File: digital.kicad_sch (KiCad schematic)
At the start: 0 parts

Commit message: new OpAmp, new RC calc, G431 added
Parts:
- added C21: 10u, symbol Device:C
- added C22, C23, C24, C25, C26, C27, C29, C31: 100n, symbol Device:C
- added C28, C30: 1u, symbol Device:C
- added C32, C33: 20p, symbol Device:C
- added J8: Conn_01x05, Connector_PinHeader_2.54mm:PinHeader_1x05_P2.54mm_Vertical, symbol Connector_Generic:Conn_01x05
- added R19: 390R, symbol Device:R
- added R20, R21, R22: 10R, symbol Device:R
- added SW1: RST, Button_Switch_SMD:SW_MEC_5GSH9, symbol Switch:SW_MEC_5E
- added U8: STM32G431RBT6, Package_QFP:LQFP-64_10x10mm_P0.5mm, symbol MCU_ST_STM32G4:STM32G431RBTx
- added Y1: Crystal, symbol Device:Crystal
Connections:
- new net: C33.1, R19.2, Y1.2
- new net: J8.1 (Pin_1), R20.2
- new net: J8.2 (Pin_2), R21.2
- new net: J8.3 (Pin_3), R22.2
- new net +3.3V: C21.1, C22.1, C23.1, C24.1, C25.1, C26.1, U8.1 (VBAT), U8.16 (VDD), U8.32 (VDD), U8.48 (VDD), U8.64 (VDD)
- new net +3.3VA: C27.1, C28.1, U8.29 (VDDA)
- new net GND: C21.2, C22.2, C23.2, C24.2, C25.2, C26.2, C27.2, C28.2, C29.2, C30.2, C31.2, C32.2, C33.2, J8.5 (Pin_5), SW1.1, SW1.2, U8.15 (VSS), U8.27 (VSSA), U8.31 (VSS), U8.47 (VSS), U8.63 (VSS)
- new net MCU_OSC_IN: C32.1, U8.5 (PF0), Y1.1
- new net MCU_OSC_OUT: R19.1, U8.6 (PF1)
- new net MCU_RST: C31.1, J8.4 (Pin_4), SW1.3 (K), SW1.4 (A), U8.7 (PG10)
- new net MCU_SWCLK: R21.1, U8.50 (PA14)
- new net MCU_SWDIO: R20.1, U8.49 (PA13)
- new net MCU_SWO: R22.1, U8.56 (PB3)
- new net mcu_vref: C29.1, C30.1, U8.28 (VREF+)

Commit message: MCU analog perephery, TL494 FB wiring
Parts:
- added FB2: FB, Inductor_SMD:L_1206_3216Metric, symbol Device:FerriteBead_Small
- added R23: 10K, symbol Device:R
- Y1: value Crystal -> 8MHz
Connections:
- net +3.3V: now also FB2.2
- net GND: now also R23.2
- net MCU_ADC_U: now reaches U8.12 (PA0)
- net MCU_ADC_I: now reaches U8.13 (PA1)
- net MCU_DAC_U: now reaches U8.18 (PA4)
- net MCU_DAC_I: now reaches U8.19 (PA5)
- net MCU_DCH: now reaches U8.24 (PB0)
- net mcu_boot0: now reaches U8.61 (PB8)
- net mcu_boot0: now also R23.1
- net +3.3VA: no longer names the net of C27.1, C28.1, U8.29 (VDDA)
- net +3.3VA: now also FB2.1

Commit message: assign footprints
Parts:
- removed R20, R21, R22: 10R, symbol Device:R
- C21, C28, C30, C32, C33: footprint (none) -> Capacitor_SMD:C_1206_3216Metric_Pad1.33x1.80mm_HandSolder
- C22, C23, C24, C25, C26, C27, C29, C31: footprint (none) -> Capacitor_SMD:C_0805_2012Metric_Pad1.18x1.45mm_HandSolder
- FB2: footprint Inductor_SMD:L_1206_3216Metric -> Inductor_SMD:L_1206_3216Metric_Pad1.22x1.90mm_HandSolder
- R19: value 390R -> 0R; footprint (none) -> Resistor_SMD:R_1206_3216Metric_Pad1.30x1.75mm_HandSolder
- R23: footprint (none) -> Resistor_SMD:R_1206_3216Metric_Pad1.30x1.75mm_HandSolder
- SW1: footprint Button_Switch_SMD:SW_MEC_5GSH9 -> Button_Switch_SMD:SW_Push_1P1T_NO_E-Switch_TL3301NxxxxxG
- Y1: footprint (none) -> Crystal:Crystal_SMD_MicroCrystal_CC1V-T1A-2Pin_8.0x3.7mm_HandSoldering
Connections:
- net MCU_SWCLK: now also J8.2 (Pin_2)
- net MCU_SWDIO: now also J8.1 (Pin_1)
- net MCU_SWO: now also J8.3 (Pin_3)
- net MCU_494_ON: now reaches U8.45 (PA11)
- no-connect marks 0 -> 39

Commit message: approximate location of the components at the PCB
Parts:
- removed SW1: RST, Button_Switch_SMD:SW_Push_1P1T_NO_E-Switch_TL3301NxxxxxG, symbol Switch:SW_MEC_5E
- added SW2: RST, Button_Switch_SMD:SW_Push_1P1T_NO_E-Switch_TL3301NxxxxxG, symbol Switch:SW_Push
- J8: value Conn_01x05 -> SWD
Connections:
- net GND: now also SW2.1
- net MCU_RST: now also J8.1 (Pin_1), SW2.2; no longer J8.4 (Pin_4)
- net MCU_SWCLK: now also J8.3 (Pin_3); no longer J8.2 (Pin_2)
- net MCU_SWDIO: now also J8.2 (Pin_2); no longer J8.1 (Pin_1)
- net MCU_SWO: now also J8.4 (Pin_4); no longer J8.3 (Pin_3)
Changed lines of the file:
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@@
 	)
 	(junction
-		(at 30.48 67.31)
-		(diameter 0)
-		(color 0 0 0 0)
-	)
-	(junction
 		(at 156.21 25.4)
 		(diameter 0)
@@
 	)
 	(junction
-		(at 43.18 67.31)
-		(diameter 0)
-		(color 0 0 0 0)
-	)
-	(junction
 		(at 95.25 25.4)
 		(diameter 0)
@@
 	(wire
 		(pts
-			(xy 30.48 67.31) (xy 30.48 69.85)
+			(xy 30.48 60.96) (xy 30.48 69.85)
 		)
 		(stroke
@@
 	(wire
 		(pts
-			(xy 31.75 67.31) (xy 30.48 67.31)
-		)
-		(stroke
-			(width 0)
-			(type default)
-		)
-	)
-	(wire
-		(pts
 			(xy 46.99 86.36) (xy 72.39 86.36)
 		)
@@
 	(wire
 		(pts
-			(xy 43.18 69.85) (xy 43.18 67.31)
+			(xy 43.18 60.96) (xy 43.18 69.85)
 		)
 		(stroke
@@
 	(wire
 		(pts
-			(xy 43.18 67.31) (xy 41.91 67.31)
-		)
-		(stroke
-			(width 0)
-			(type default)
-		)
-	)
-	(wire
-		(pts
 			(xy 46.99 101.6) (xy 41.91 101.6)
 		)
@@
 	(wire
 		(pts
-			(xy 30.48 60.96) (xy 30.48 67.31)
-		)
-		(stroke
-			(width 0)
-			(type default)
-		)
-	)
-	(wire
-		(pts
 			(xy 134.62 25.4) (xy 143.51 25.4)
 		)
@@
 		)
 	)
-	(wire
-		(pts
-			(xy 43.18 67.31) (xy 43.18 60.96)
-		)
-		(stroke
-			(width 0)
-			(type default)
-		)
-	)
 	(label "mcu_boot0"
 		(at 157.48 120.65 0)
@@
 	(global_label "MCU_SWO"
 		(shape input)
-		(at 238.76 31.75 180)
+		(at 238.76 34.29 180)
 		(fields_autoplaced yes)
 		(effects
@@
 		)
 		(property "Intersheetrefs" "${INTERSHEET_REFS}"
-			(at 226.7639 31.75 0)
+			(at 226.7639 34.29 0)
 			(effects
 				(font
@@
 	(global_label "MCU_SWDIO"
 		(shape input)
-		(at 238.76 26.67 180)
+		(at 238.76 29.21 180)
 		(fields_autoplaced yes)
 		(effects
@@
 		)
 		(property "Intersheetrefs" "${INTERSHEET_REFS}"
-			(at 224.8891 26.67 0)
+			(at 224.8891 29.21 0)
 			(effects
 				(font
@@
 	(global_label "MCU_SWCLK"
 		(shape input)
-		(at 238.76 29.21 180)
+		(at 238.76 31.75 180)
 		(fields_autoplaced yes)
 		(effects
@@
 		)
 		(property "Intersheetrefs" "${INTERSHEET_REFS}"
-			(at 224.5263 29.21 0)
+			(at 224.5263 31.75 0)
 			(effects
 				(font
@@
 	(global_label "MCU_RST"
 		(shape input)
-		(at 238.76 34.29 180)
+		(at 238.76 26.67 180)
 		(fields_autoplaced yes)
 		(effects
@@
 		)
 		(property "Intersheetrefs" "${INTERSHEET_REFS}"
-			(at 227.3082 34.29 0)
+			(at 227.3082 26.67 0)
 			(effects
 				(font
@@
 	)
 	(symbol
+		(lib_id "Switch:SW_Push")
+		(at 36.83 69.85 0)
+		(unit 1)
+		(exclude_from_sim no)
+		(in_bom yes)
+		(on_board yes)
+		(dnp no)
+		(fields_autoplaced yes)
+		(property "Reference" "SW2"
+			(at 36.83 62.23 0)
+			(effects
+				(font
+					(size 1.27 1.27)
+				)
+			)
+		)
+		(property "Value" "RST"
+			(at 36.83 64.77 0)
+			(effects
+				(font
+					(size 1.27 1.27)
+				)
+			)
+		)
+		(property "Footprint" "Button_Switch_SMD:SW_Push_1P1T_NO_E-Switch_TL3301NxxxxxG"
+			(at 36.83 64.77 0)
+			(effects
+				(font
+					(size 1.27 1.27)
+				)
+				(hide yes)
+			)
+		)
+		(property "Datasheet" "~"
+			(at 36.83 64.77 0)
+			(effects
+				(font
+					(size 1.27 1.27)
+				)
+				(hide yes)
+			)
+		)
+		(property "Description" "Push button switch, generic, two pins"
+			(at 36.83 69.85 0)
+			(effects
+				(font
+					(size 1.27 1.27)
+				)
+				(hide yes)
+			)
+		)
+		(pin "1"
+		)
+		(pin "2"
+		)
+		(instances
+			(project ""
+				(path "/485c2fed-5176-4ba8-b79d-ac7eddb44491/422ff71a-ee59-41d3-a8e4-e6d2465802f7"
+					(reference "SW2")
+					(unit 1)
+				)
+			)
+		)
+	)
+	(symbol
 		(lib_id "Device:C")
 		(at 68.58 62.23 0)
@@
 			)
 		)
-		(property "Value" "Conn_01x05"
+		(property "Value" "SWD"
 			(at 252.73 33.0199 0)
 			(effects
@@
 					(unit 1)
 				)
-			)
-		)
-	)
-	(symbol
-		(lib_id "Switch:SW_MEC_5E")
-		(at 36.83 69.85 0)
-		(unit 1)
-		(exclude_from_sim no)
-		(in_bom yes)
-		(on_board yes)
-		(dnp no)
-		(property "Reference" "SW1"
-			(at 34.798 71.628 0)
-			(effects
-				(font
-					(size 1.27 1.27)
-				)
-				(justify left)
-			)
-		)
-		(property "Value" "RST"
-			(at 34.798 74.168 0)
-			(effects
-				(font
-					(size 1.27 1.27)
-				)
-				(justify left)
-			)
-		)
-		(property "Footprint" "Button_Switch_SMD:SW_Push_1P1T_NO_E-Switch_TL3301NxxxxxG"
-			(at 36.83 62.23 0)
-			(effects
-				(font
-					(size 1.27 1.27)
-				)
-				(hide yes)
-			)
-		)
-		(property "Datasheet" "http://www.apem.com/int/index.php?controller=attachment&id_attachment=1371"
-			(at 36.83 62.23 0)
-			(effects
-				(font
-					(size 1.27 1.27)
-				)
-				(hide yes)
-			)
-		)
-		(property "Description" "MEC 5E single pole normally-open tactile switch"
-			(at 36.83 69.85 0)
-			(effects
-				(font
-					(size 1.27 1.27)
-				)
-				(hide yes)
-			)
-		)
-		(pin "4"
-		)
-		(pin "1"
-		)
-		(pin "2"
-		)
-		(pin "3"
-		)
-		(instances
-			(project ""
-				(path "/485c2fed-5176-4ba8-b79d-ac7eddb44491/422ff71a-ee59-41d3-a8e4-e6d2465802f7"
-					(reference "SW1")
-					(unit 1)
-				)

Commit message: final location of the power,analog sections
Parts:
- removed SW2: RST, Button_Switch_SMD:SW_Push_1P1T_NO_E-Switch_TL3301NxxxxxG, symbol Switch:SW_Push
- added JP1: RST, TestPoint:TestPoint_2Pads_Pitch2.54mm_Drill0.8mm, symbol Jumper:Jumper_2_Open
- Y1: footprint Crystal:Crystal_SMD_MicroCrystal_CC1V-T1A-2Pin_8.0x3.7mm_HandSoldering -> Crystal:Crystal_SMD_0603-2Pin_6.0x3.5mm_HandSoldering
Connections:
- net GND: now also JP1.1 (A)
- net MCU_494_ON: now also U8.13 (PA1); no longer U8.45 (PA11)
- net MCU_ADC_I: now also U8.20 (PA6); no longer U8.13 (PA1)
- net MCU_ADC_U: now also U8.21 (PA7); no longer U8.12 (PA0)
- net MCU_DCH: now also U8.33 (PB11); no longer U8.24 (PB0)
- net MCU_RST: now also JP1.2 (B)
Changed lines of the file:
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@@
+	)
+	(no_connect
+		(at 144.78 57.15)
 	)
 	(no_connect
@@
 	)
 	(no_connect
+		(at 144.78 85.09)
+	)
+	(no_connect
 		(at 144.78 87.63)
 	)
@@
 	)
 	(no_connect
-		(at 144.78 74.93)
-	)
-	(no_connect
 		(at 144.78 80.01)
 	)
@@
 	)
 	(no_connect
-		(at 144.78 128.27)
-	)
-	(no_connect
 		(at 144.78 77.47)
 	)
@@
 	)
 	(no_connect
-		(at 144.78 72.39)
-	)
-	(no_connect
 		(at 144.78 105.41)
 	)
@@
 		(at 109.22 107.95)
 	)
+	(no_connect
+		(at 144.78 100.33)
+	)
 	(wire
 		(pts
@@
 	(wire
 		(pts
+			(xy 144.78 59.69) (xy 148.59 59.69)
+		)
+		(stroke
+			(width 0)
+			(type default)
+		)
+	)
+	(wire
+		(pts
 			(xy 238.76 34.29) (xy 245.11 34.29)
 		)
@@
 	(wire
 		(pts
-			(xy 144.78 59.69) (xy 148.59 59.69)
-		)
-		(stroke
-			(width 0)
-			(type default)
-		)
-	)
-	(wire
-		(pts
 			(xy 43.18 54.61) (xy 40.64 54.61)
 		)
@@
 	(wire
 		(pts
+			(xy 144.78 72.39) (xy 148.59 72.39)
+		)
+		(stroke
+			(width 0)
+			(type default)
+		)
+	)
+	(wire
+		(pts
 			(xy 132.08 45.72) (xy 129.54 45.72)
 		)
@@
 	(wire
 		(pts
+			(xy 144.78 74.93) (xy 148.59 74.93)
+		)
+		(stroke
+			(width 0)
+			(type default)
+		)
+	)
+	(wire
+		(pts
 			(xy 127 147.32) (xy 127 148.59)
 		)
@@
 	(wire
 		(pts
-			(xy 144.78 85.09) (xy 148.59 85.09)
-		)
-		(stroke
-			(width 0)
-			(type default)
-		)
-	)
-	(wire
-		(pts
 			(xy 143.51 33.02) (xy 149.86 33.02)
 		)
@@
 	(wire
 		(pts
-			(xy 144.78 100.33) (xy 148.59 100.33)
-		)
-		(stroke
-			(width 0)
-			(type default)
-		)
-	)
-	(wire
-		(pts
 			(xy 50.8 101.6) (xy 46.99 101.6)
 		)
@@
 	(wire
 		(pts
+			(xy 144.78 128.27) (xy 148.59 128.27)
+		)
+		(stroke
+			(width 0)
+			(type default)
+		)
+	)
+	(wire
+		(pts
 			(xy 144.78 120.65) (xy 175.26 120.65)
 		)
@@
 		(pts
 			(xy 95.25 25.4) (xy 106.68 25.4)
-		)
-		(stroke
-			(width 0)
-			(type default)
-		)
-	)
-	(wire
-		(pts
-			(xy 144.78 57.15) (xy 148.59 57.15)
 		)
 		(stroke
@@
 	(global_label "MCU_ADC_U"
 		(shape input)
-		(at 148.59 57.15 0)
+		(at 148.59 74.93 0)
 		(fields_autoplaced yes)
 		(effects
@@
 		)
 		(property "Intersheetrefs" "${INTERSHEET_REFS}"
-			(at 162.5214 57.15 0)
+			(at 162.5214 74.93 0)
 			(effects
 				(font
@@
 	(global_label "MCU_ADC_I"
 		(shape input)
-		(at 148.59 59.69 0)
+		(at 148.59 72.39 0)
 		(fields_autoplaced yes)
 		(effects
@@
 		)
 		(property "Intersheetrefs" "${INTERSHEET_REFS}"
-			(at 161.7957 59.69 0)
+			(at 161.7957 72.39 0)
 			(effects
 				(font
@@
 	(global_label "MCU_DCH"
 		(shape input)
-		(at 148.59 100.33 0)
+		(at 148.59 128.27 0)
 		(fields_autoplaced yes)
 		(effects
@@
 		)
 		(property "Intersheetrefs" "${INTERSHEET_REFS}"
-			(at 160.4652 100.33 0)
+			(at 160.4652 128.27 0)
 			(effects
 				(font
@@
 	(global_label "MCU_494_ON"
 		(shape input)
-		(at 148.59 85.09 0)
+		(at 148.59 59.69 0)
 		(fields_autoplaced yes)
 		(effects
@@
 		)
 		(property "Intersheetrefs" "${INTERSHEET_REFS}"
-			(at 163.8518 85.09 0)
+			(at 163.8518 59.69 0)
 			(effects
 				(font
@@
 	)
 	(symbol
+		(lib_id "Jumper:Jumper_2_Open")
+		(at 36.83 69.85 0)
+		(unit 1)
+		(exclude_from_sim no)
+		(in_bom yes)
+		(on_board yes)
+		(dnp no)
+		(fields_autoplaced yes)
+		(property "Reference" "JP1"
+			(at 36.83 63.5 0)
+			(effects
+				(font
+					(size 1.27 1.27)
+				)
+			)
+		)
+		(property "Value" "RST"
+			(at 36.83 66.04 0)
+			(effects
+				(font
+					(size 1.27 1.27)
+				)
+			)
+		)
+		(property "Footprint" "TestPoint:TestPoint_2Pads_Pitch2.54mm_Drill0.8mm"
+			(at 36.83 69.85 0)
+			(effects
+				(font
+					(size 1.27 1.27)
+				)
+				(hide yes)
+			)
+		)
+		(property "Datasheet" "~"
+			(at 36.83 69.85 0)
+			(effects
+				(font
+					(size 1.27 1.27)
+				)
+				(hide yes)
+			)
+		)
+		(property "Description" "Jumper, 2-pole, open"
+			(at 36.83 69.85 0)
+			(effects
+				(font
+					(size 1.27 1.27)
+				)
+				(hide yes)
+			)
+		)
+		(pin "1"
+		)
+		(pin "2"
+		)
+		(instances
+			(project ""
+				(path "/485c2fed-5176-4ba8-b79d-ac7eddb44491/422ff71a-ee59-41d3-a8e4-e6d2465802f7"
+					(reference "JP1")
+					(unit 1)
+				)
+			)
+		)
+	)
+	(symbol
 		(lib_id "Device:R")
 		(at 175.26 129.54 0)
@@
 			)
 		)
-		(property "Footprint" "Crystal:Crystal_SMD_MicroCrystal_CC1V-T1A-2Pin_8.0x3.7mm_HandSoldering"
+		(property "Footprint" "Crystal:Crystal_SMD_0603-2Pin_6.0x3.5mm_HandSoldering"
 			(at 46.99 93.98 0)
 			(effects
@@
 					(unit 1)
 				)
-			)
-		)
-	)
-	(symbol
-		(lib_id "Switch:SW_Push")
-		(at 36.83 69.85 0)
-		(unit 1)
-		(exclude_from_sim no)
-		(in_bom yes)
-		(on_board yes)
-		(dnp no)
-		(fields_autoplaced yes)
-		(property "Reference" "SW2"
-			(at 36.83 62.23 0)
-			(effects
-				(font
-					(size 1.27 1.27)
-				)
-			)
-		)
-		(property "Value" "RST"
-			(at 36.83 64.77 0)
-			(effects
-				(font
-					(size 1.27 1.27)
-				)
-			)
-		)
-		(property "Footprint" "Button_Switch_SMD:SW_Push_1P1T_NO_E-Switch_TL3301NxxxxxG"
-			(at 36.83 64.77 0)
-			(effects
-				(font
-					(size 1.27 1.27)
-				)
-				(hide yes)
-			)
-		)
-		(property "Datasheet" "~"
-			(at 36.83 64.77 0)
-			(effects
-				(font
-					(size 1.27 1.27)
-				)
-				(hide yes)
-			)
-		)
-		(property "Description" "Push button switch, generic, two pins"
-			(at 36.83 69.85 0)
-			(effects
-				(font
-					(size 1.27 1.27)
-				)
-				(hide yes)
-			)
-		)
-		(pin "1"
-		)
-		(pin "2"
-		)
-		(instances
-			(project ""
-				(path "/485c2fed-5176-4ba8-b79d-ac7eddb44491/422ff71a-ee59-41d3-a8e4-e6d2465802f7"
-					(reference "SW2")
-					(unit 1)
-				)

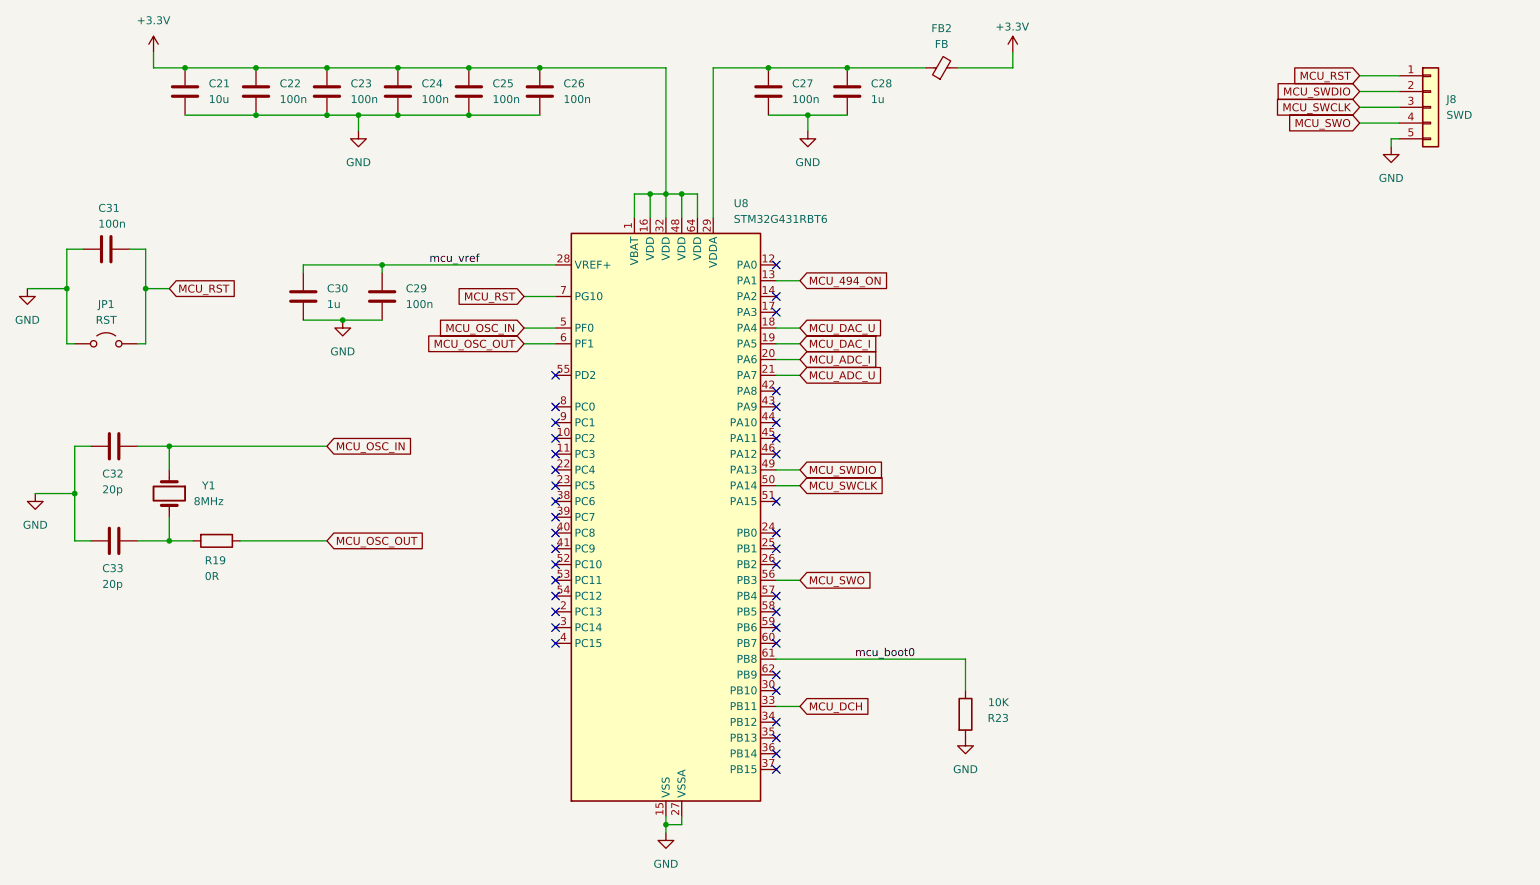
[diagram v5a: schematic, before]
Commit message: added display and encoders signal lines, hints
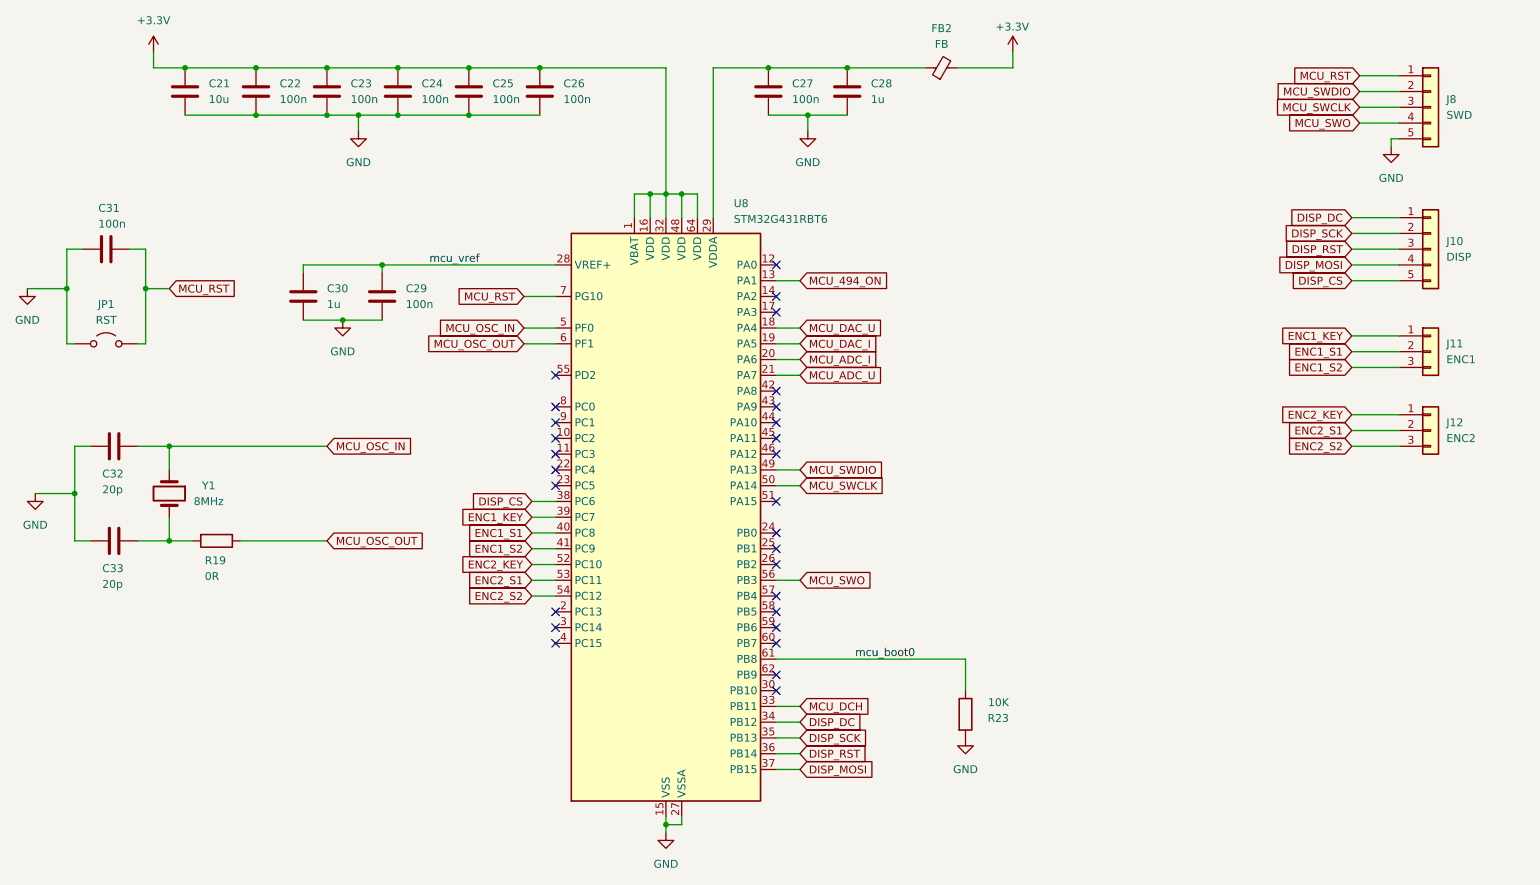
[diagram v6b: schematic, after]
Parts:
- added J10: DISP, Connector_PinHeader_2.54mm:PinHeader_1x05_P2.54mm_Vertical, symbol Connector_Generic:Conn_01x05
- added J11: ENC1, Connector_PinHeader_2.54mm:PinHeader_1x03_P2.54mm_Vertical, symbol Connector_Generic:Conn_01x03
- added J12: ENC2, Connector_PinHeader_2.54mm:PinHeader_1x03_P2.54mm_Vertical, symbol Connector_Generic:Conn_01x03
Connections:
- net DISP_DC: now reaches U8.34 (PB12)
- net DISP_DC: now also J10.1 (Pin_1)
- net DISP_SCK: now reaches U8.35 (PB13)
- net DISP_SCK: now also J10.2 (Pin_2)
- net DISP_RST: now reaches U8.36 (PB14)
- net DISP_RST: now also J10.3 (Pin_3)
- net DISP_MOSI: now reaches U8.37 (PB15)
- net DISP_MOSI: now also J10.4 (Pin_4)
- net DISP_CS: now reaches U8.38 (PC6)
- net DISP_CS: now also J10.5 (Pin_5)
- net ENC1_KEY: now reaches U8.39 (PC7)
- net ENC1_KEY: now also J11.1 (Pin_1)
- net ENC1_S1: now reaches U8.40 (PC8)
- net ENC1_S1: now also J11.2 (Pin_2)
- net ENC1_S2: now reaches U8.41 (PC9)
- net ENC1_S2: now also J11.3 (Pin_3)
- net ENC2_KEY: now reaches U8.52 (PC10)
- net ENC2_KEY: now also J12.1 (Pin_1)
- net ENC2_S1: now reaches U8.53 (PC11)
- net ENC2_S1: now also J12.2 (Pin_2)
- net ENC2_S2: now reaches U8.54 (PC12)
- net ENC2_S2: now also J12.3 (Pin_3)
- no-connect marks 39 -> 28
